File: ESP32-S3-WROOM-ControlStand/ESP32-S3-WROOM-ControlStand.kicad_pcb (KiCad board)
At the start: 2 copper layers, 199.4 x 126.4 mm, 188 parts, among them IC601 USBLC6-2SC6, J1 Button & LED Panel, J10 RJ45, J101 Keypad Panel, J11 Barrel_Jack, J12 Battery, J2 Button & LED Panel, J3 STEMMA (Display), J4 Horn, J5 Brake, J6 Light Switch, J601 GCT_USB4105, J7 Reverser, J8 Throttle, J9 RJ45, P1 CONN_8, P2 Misc buttons, bell, status LED, P6 CONN_3, P7 CONN_3, P701 CONN_5, P8 CONN_5, P9 CONN_5, SW1 A, SW10 SW_PUSH_SMALL, SW11 SW_PUSH_SMALL, SW12 SW_PUSH_SMALL, SW13 SW_PUSH_SMALL, SW14 SW_PUSH_SMALL, SW15 SW_PUSH_SMALL, SW16 SW_PUSH_SMALL, SW17 SW_PUSH_SMALL, SW18 SW_PUSH_SMALL, SW19 SW_PUSH_SMALL, SW2 B, SW20 SW_PUSH_SMALL, SW21 SW_PUSH_SMALL, SW22 SW_PUSH_SMALL, SW23 On/Off, SW24 RESET, SW3 C, SW4 D, SW5 Bell, SW601 BOOT, SW7 SW_PUSH_SMALL, SW701 "1", SW702 "4", SW703 "7", SW704 "*", SW705 "2", SW706 "5", SW707 "8", SW708 "0", SW709 "3", SW710 "6", SW711 "9", SW712 "#", SW8 SW_PUSH_SMALL, SW9 SW_PUSH_SMALL, T1 Buttons, T2 LEDS, T3 Buttons, T4 LEDS, T5 + 15 in -, T6 + 15 out -, U1 MCP23017, U2 TBD62083A, U3 MCP23017, U4 TBD62083A, U5 TCAN332DR, U6 MCP73871, U601 ESP32_S3_WROOM-1, U7 LM2574HVM-5.0, U701 TCA8418, U8 TC1263-3.3VOATR

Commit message: Snapshot April 8, 2024.
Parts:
- removed C1, C2, C3: .1 uf, Capacitors_SMD:C_0603
- removed C13: 22 uf 100V, Capacitors_SMD:CP_Elec_8x10
- removed C4: 15 uf 63V, Capacitors_SMD:CP_Elec_4x5.7
- removed C5: 47 nf, Capacitors_SMD:C_0603
- removed C8: 220 uf 25V, Capacitors_SMD:CP_Elec_8x10
- removed D10, D11, D12, D13, D14, D15, D16, D17, D2, D3, D4, D5, D6, D7, D8, D9: LED, LEDs:LED_D5.0mm
- removed D18, D19, D25: DFLS240-7, Diodes_SMD:D_PowerDI-123
- removed D27: SB160-E3/54, Diodes_SMD:D_SMB
- removed FD2: FidMark, Fiducials:Fiducial_1mm_Dia_2.54mm_Outer_CopperTop
- removed J1, J2: Button & LED Panel, Pin_Headers:Pin_Header_Straight_1x05_Pitch2.54mm
- removed J10, J9: RJ45, RJ45-8N-S:RJ45_8N-S
- removed JP1: Termination, Pin_Headers:Pin_Header_Straight_2x02_Pitch2.54mm
- removed L1: 330 uh, SRN1060:SRN1060
- removed MK10, MK11, MK12, MK13, MK14, MK15, MK16, MK9: Mounting_Hole, Mounting_Holes:MountingHole_2.5mm
- removed P8, P9: CONN_5, Pin_Headers:Pin_Header_Angled_1x05_Pitch2.54mm
- removed R10, R11: 60 Ohms, Resistors_SMD:R_1206
- removed R7, R8, R9: 10K, Resistors_SMD:R_0402
- removed the REF*** at (191.6, 139.1)
- removed RP1, RP2: 330, 48xxP:4816P
- removed SW10, SW11, SW12, SW13, SW14, SW15, SW16, SW17, SW18, SW19, SW20, SW21, SW22, SW7, SW8, SW9: SW_PUSH_SMALL, Buttons_Switches_THT:SW_PUSH_6mm
- removed T1: Buttons, Terminal_Blocks:TerminalBlock_Pheonix_MPT-2.54mm_9pol
- removed T2, T4: LEDS, Connectors_Terminal_Blocks:TerminalBlock_Pheonix_MPT-2.54mm_9pol
- removed T3: Buttons, Connectors_Terminal_Blocks:TerminalBlock_Pheonix_MPT-2.54mm_9pol
- removed T5: + 15 in -, Terminal_Blocks:TerminalBlock_Pheonix_MPT-2.54mm_2pol
- removed T6: + 15 out -, Terminal_Blocks:TerminalBlock_Pheonix_MPT-2.54mm_2pol
- removed U1, U3: MCP23017, Housings_SOIC:SOIC-28W_7.5x17.9mm_Pitch1.27mm
- removed U2, U4: TBD62083A, Housings_SOIC:SOIC-18W_7.5x11.6mm_Pitch1.27mm
- removed U5: TCAN332DR, Housings_SOIC:SOIC-8_3.9x4.9mm_Pitch1.27mm
- removed U7: LM2574HVM-5.0, SOIC_Wide:SOIC-14_7.4x8.7mm_Pitch1.27mm
- added REF**: KiCad-Logo2_5mm_SilkScreen, Symbol:KiCad-Logo2_5mm_SilkScreen, F.Cu at (165.2, 128.0)
- J3: value STEMMA (Display) -> Display
- P1: value CONN_8 -> To Main Board
- P6, P7: value CONN_3 -> To Main Board
- P701: value CONN_5 -> To Main Board
- moved MK702 115.1 mm to (111.3, 74.8)
- moved MK704 115.1 mm to (111.3, 36.7)
- moved P701 115.1 mm to (126.5, 38.0)
- moved R701 115.1 mm to (120.8, 41.8)
- moved SW701 115.1 mm to (115.9, 56.6)
- moved SW702 115.1 mm to (115.9, 61.7)
- moved SW703 115.1 mm to (115.9, 66.7)
- moved SW704 115.1 mm to (115.9, 71.8)
- moved SW709 115.1 mm to (126.1, 56.6)
- moved SW710 115.1 mm to (126.1, 61.7)
- moved SW711 115.1 mm to (126.1, 66.7)
- moved SW712 115.1 mm to (126.1, 71.8)
- moved U701 115.1 mm to (119.5, 48.1)
- moved C701 115.1 mm to (119.9, 43.6)
- moved MK701 115.1 mm to (131.6, 74.8)
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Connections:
- J11 pad 3: Net-(J11-Pad3) -> unconnected-(J11-Pad3)
- J601 pad A8: Net-(J601-PadA8) -> unconnected-(J601-PadA8)
- J601 pad B8: Net-(J601-PadB8) -> unconnected-(J601-PadB8)
- MK20 pad 1: Net-(MK20-Pad1) -> unconnected-(MK20-Pad1)
- P701 pad 1: Net-(P701-Pad1) -> unconnected-(P701-Pad1)
- SW23 pad 3: Net-(SW23-Pad3) -> unconnected-(SW23-Pad3)
- U601 pad 28: Net-(U601-Pad28) -> unconnected-(U601-Pad28)
- U601 pad 29: Net-(U601-Pad29) -> unconnected-(U601-Pad29)
- U601 pad 30: Net-(U601-Pad30) -> unconnected-(U601-Pad30)
- U601 pad 32: Net-(U601-Pad32) -> unconnected-(U601-Pad32)
- U601 pad 33: Net-(U601-Pad33) -> unconnected-(U601-Pad33)
- U601 pad 34: Net-(U601-Pad34) -> unconnected-(U601-Pad34)
- U601 pad 35: Net-(U601-Pad35) -> unconnected-(U601-Pad35)
- U601 pad 36: Net-(U601-Pad36) -> unconnected-(U601-Pad36)
- U601 pad 37: Net-(U601-Pad37) -> unconnected-(U601-Pad37)
- U601 pad 39: Net-(U601-Pad39) -> unconnected-(U601-Pad39)
- U601 pad 6: Net-(U601-Pad6) -> unconnected-(U601-Pad6)
- U701 pad 1: Net-(U701-Pad1) -> unconnected-(U701-Pad1)
- U701 pad 13: Net-(U701-Pad13) -> unconnected-(U701-Pad13)
- U701 pad 14: Net-(U701-Pad14) -> unconnected-(U701-Pad14)
- U701 pad 15: Net-(U701-Pad15) -> unconnected-(U701-Pad15)
- U701 pad 16: Net-(U701-Pad16) -> unconnected-(U701-Pad16)
- U701 pad 17: Net-(U701-Pad17) -> unconnected-(U701-Pad17)
- U701 pad 18: Net-(U701-Pad18) -> unconnected-(U701-Pad18)
- U701 pad 2: Net-(U701-Pad2) -> unconnected-(U701-Pad2)
- U701 pad 24: Net-(U701-Pad24) -> unconnected-(U701-Pad24)
- U701 pad 3: Net-(U701-Pad3) -> unconnected-(U701-Pad3)
- U701 pad 4: Net-(U701-Pad4) -> unconnected-(U701-Pad4)
- U8 pad 3: Net-(U8-Pad3) -> unconnected-(U8-Pad3)
- U8 pad 5: Net-(U8-Pad5) -> unconnected-(U8-Pad5)
- U8 pad 7: Net-(U8-Pad7) -> unconnected-(U8-Pad7)
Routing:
- net +BATT: track 222.2 -> 0.00 mm, vias 4 -> 0
- net Net-(D17-Pad2): track 111.1 -> 0.00 mm, vias 3 -> 0
- net +12V: track 99.1 -> 0.00 mm, vias 5 -> 0
- net GND: track 279.0 -> 183.9 mm, vias 56 -> 45
- net /CAN_TX: track 90.3 -> 0.00 mm, vias 4 -> 0
- net /CAN_RX: track 90.1 -> 0.00 mm, vias 4 -> 0
- net Net-(SW15-Pad1): track 87.3 -> 0.00 mm, vias 3 -> 0
- net Net-(D9-Pad2): track 85.8 -> 0.00 mm, vias 3 -> 0
- net Net-(SW7-Pad1): track 82.7 -> 0.00 mm, vias 3 -> 0
- net Net-(SW16-Pad1): track 79.2 -> 0.00 mm, vias 4 -> 0
- net Net-(D16-Pad2): track 78.8 -> 0.00 mm, vias 2 -> 0
- net Net-(D8-Pad2): track 76.3 -> 0.00 mm, vias 3 -> 0
- net Net-(SW8-Pad1): track 74.4 -> 0.00 mm, vias 3 -> 0
- net Net-(SW17-Pad1): track 71.4 -> 0.00 mm, vias 4 -> 0
- net Net-(D7-Pad2): track 70.2 -> 0.00 mm, vias 3 -> 0
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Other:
- board size 199.4 x 126.4 mm -> 127 x 118.9 mm
- net class Default removed

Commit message: Snapshot April 8, 2024.
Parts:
- moved MK18 14.7 mm to (160.1, 143.7)
- moved J8 14.7 mm to (140.0, 126.7)
- moved MK19 14.7 mm to (160.1, 99.3)
- moved REF*** 14.7 mm to (153.5, 131.2)
- moved C12 14.7 mm to (110.4, 130.9)
- moved D22 14.7 mm to (89.7, 126.4)
- moved D23 14.7 mm to (91.0, 126.4)
- moved J12 14.7 mm to (81.6, 129.0)
- moved MK17 14.7 mm to (102.9, 143.7)
- moved R1 14.7 mm to (106.5, 134.7)
- moved R30 14.7 mm to (115.2, 124.5)
- moved SW703 14.7 mm to (102.0, 61.9)
- moved SW707 14.7 mm to (107.1, 61.9)
- moved C29 14.7 mm to (121.8, 126.6)
- moved C6 14.7 mm to (86.9, 113.5)
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
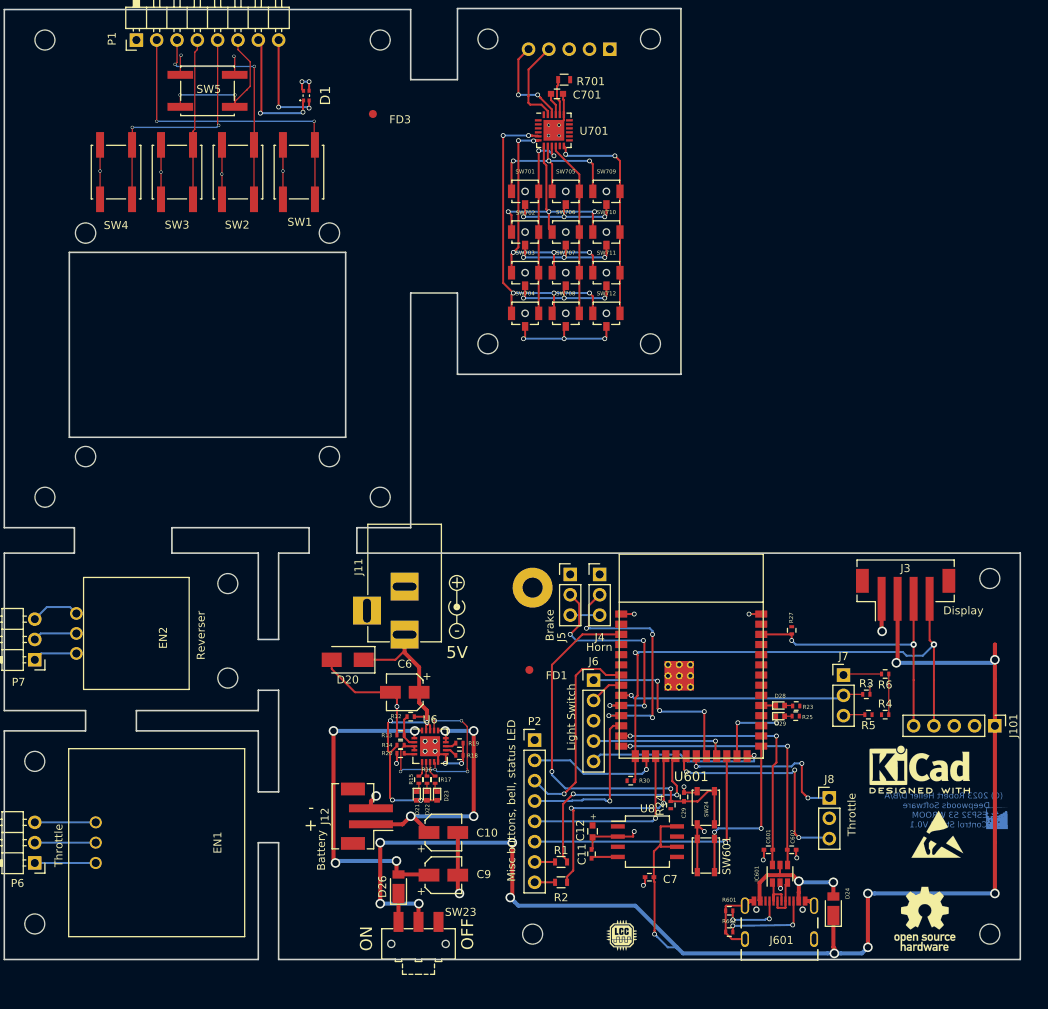
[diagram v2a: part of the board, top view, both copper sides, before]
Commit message: 3D models mostly done.
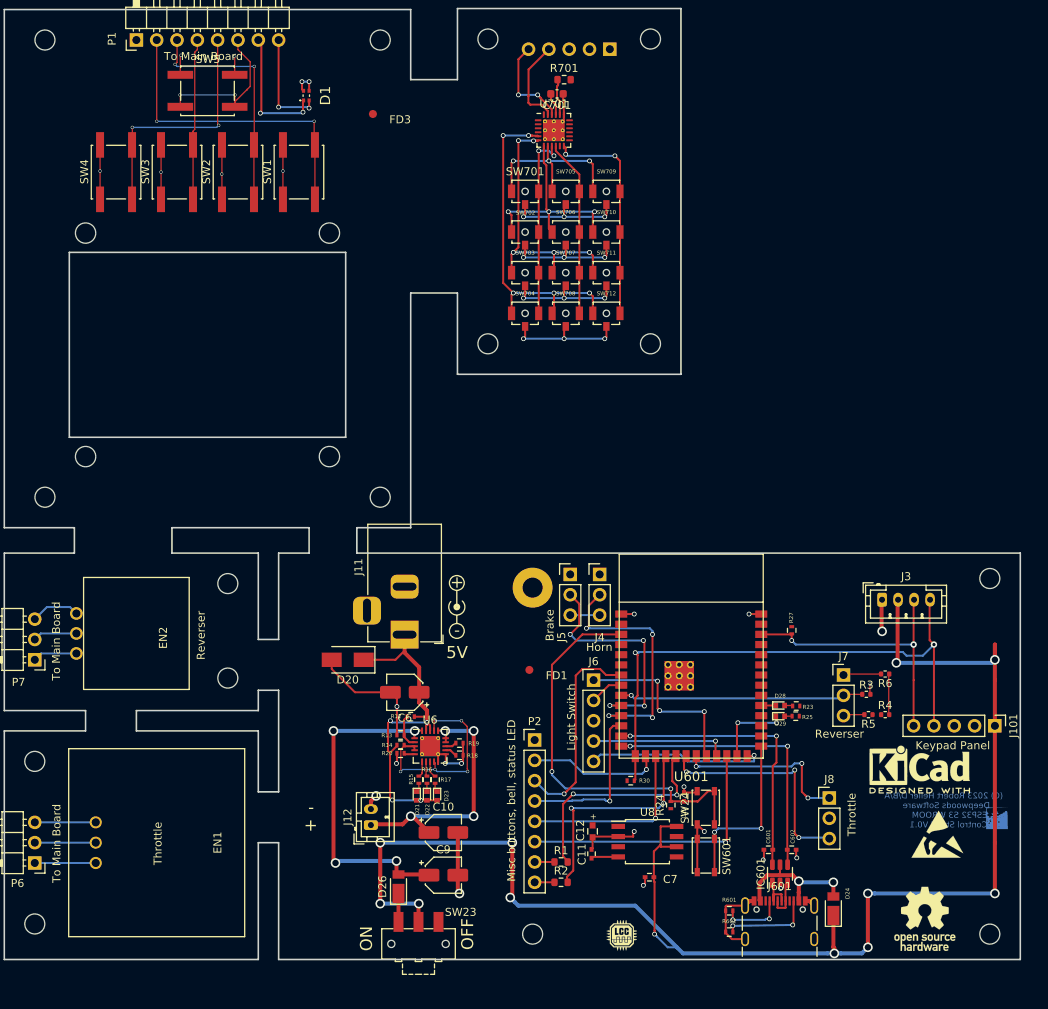
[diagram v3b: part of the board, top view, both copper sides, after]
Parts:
- C10, C6, C9: footprint Capacitors_SMD:CP_Elec_4x5.7 -> Capacitor_SMD:CP_Elec_4x5.7
- C701: footprint Capacitors_SMD:C_0603 -> Capacitor_SMD:C_0603_1608Metric
- IC601: footprint TO_SOT_Packages_SMD:SOT-23-6 -> Package_TO_SOT_SMD:SOT-23-6
- J11: footprint Connectors:BARREL_JACK -> Connector_BarrelJack:BarrelJack_Horizontal
- J12: footprint Connectors_JST:JST_PH_B2B-PH-SM4-TB_02x2.00mm_Straight -> Connector_JST:JST_PH_B2B-PH-K_1x02_P2.00mm_Vertical
- J3: footprint Connectors_JST:JST_PH_B4B-PH-SM4-TB_04x2.00mm_Straight -> Connector_JST:JST_PH_B4B-PH-K_1x04_P2.00mm_Vertical
- J601: footprint GCT_USB:GCT_USB4105-GF-A -> Connector_USB:USB_C_Receptacle_GCT_USB4105-xx-A_16P_TopMnt_Horizontal
- R1, R2, R701: footprint Resistors_SMD:R_0603 -> Resistor_SMD:R_0603_1608Metric
- R3, R4, R5, R6: footprint Resistors_SMD:R_0402 -> Resistor_SMD:R_0402_1005Metric
- SW1, SW2, SW3, SW4, SW5: footprint Buttons_Switches_SMD:SW_SPST_EVQQ2 -> Button_Switch_SMD:SW_SPST_EVQQ2
- SW24: footprint Buttons_Switches_SMD:SW_SPST_PTS810 -> Button_Switch_SMD:SW_SPST_PTS810
- SW701: footprint Buttons_Switches_SMD:SW_SPST_B3U-1100P-B -> Button_Switch_SMD:SW_SPST_B3U-1100P-B
- U6: footprint Housings_DFN_QFN:QFN-20-1EP_4x4mm_Pitch0.5mm -> Package_DFN_QFN:QFN-20-1EP_4x4mm_P0.5mm_EP2.5x2.5mm_ThermalVias
- U701: footprint Housings_DFN_QFN:QFN-24-1EP_4x4mm_Pitch0.5mm -> Package_DFN_QFN:QFN-24-1EP_4x4mm_P0.5mm_EP2.7x2.7mm_ThermalVias
- U8: footprint Housings_SOIC:SO-8_5.3x6.2mm_Pitch1.27mm -> Package_SO:SOIC-8W_5.3x5.3mm_P1.27mm
- moved J3 3.19 mm to (146.6, 101.9)
- moved J12 1.57 mm to (82.7, 130.1)
- moved J601 1.09 mm to (133.8, 143.2)
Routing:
- net GND: vias 45 -> 37
